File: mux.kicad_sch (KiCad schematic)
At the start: 11 parts, among them M1 SN74LV4051ADYYR, M10 SN74LV4051ADYYR, M11 SN74LV4051ADYYR, M2 SN74LV4051ADYYR, M3 SN74LV4051ADYYR, M4 SN74LV4051ADYYR, M5 SN74LV4051ADYYR, M6 SN74LV4051ADYYR, M7 SN74LV4051ADYYR, M8 SN74LV4051ADYYR, M9 SN74LV4051ADYYR

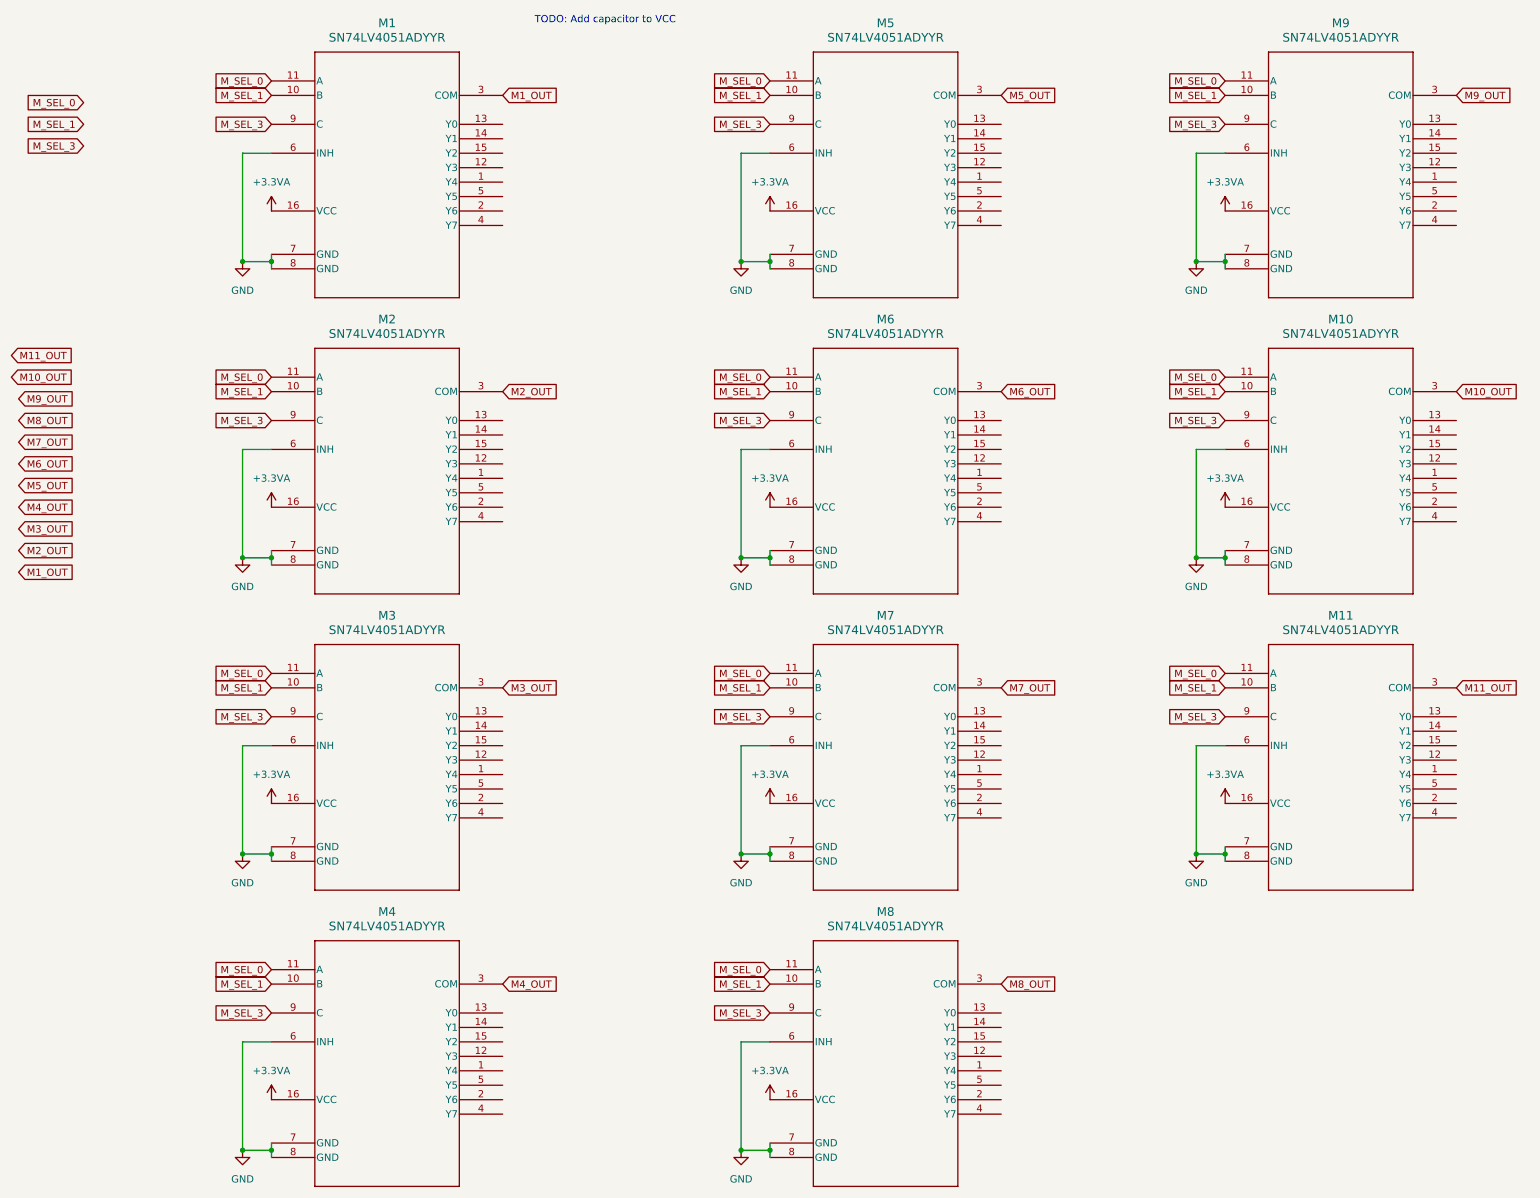
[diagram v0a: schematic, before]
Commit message: start keyboard switch layout
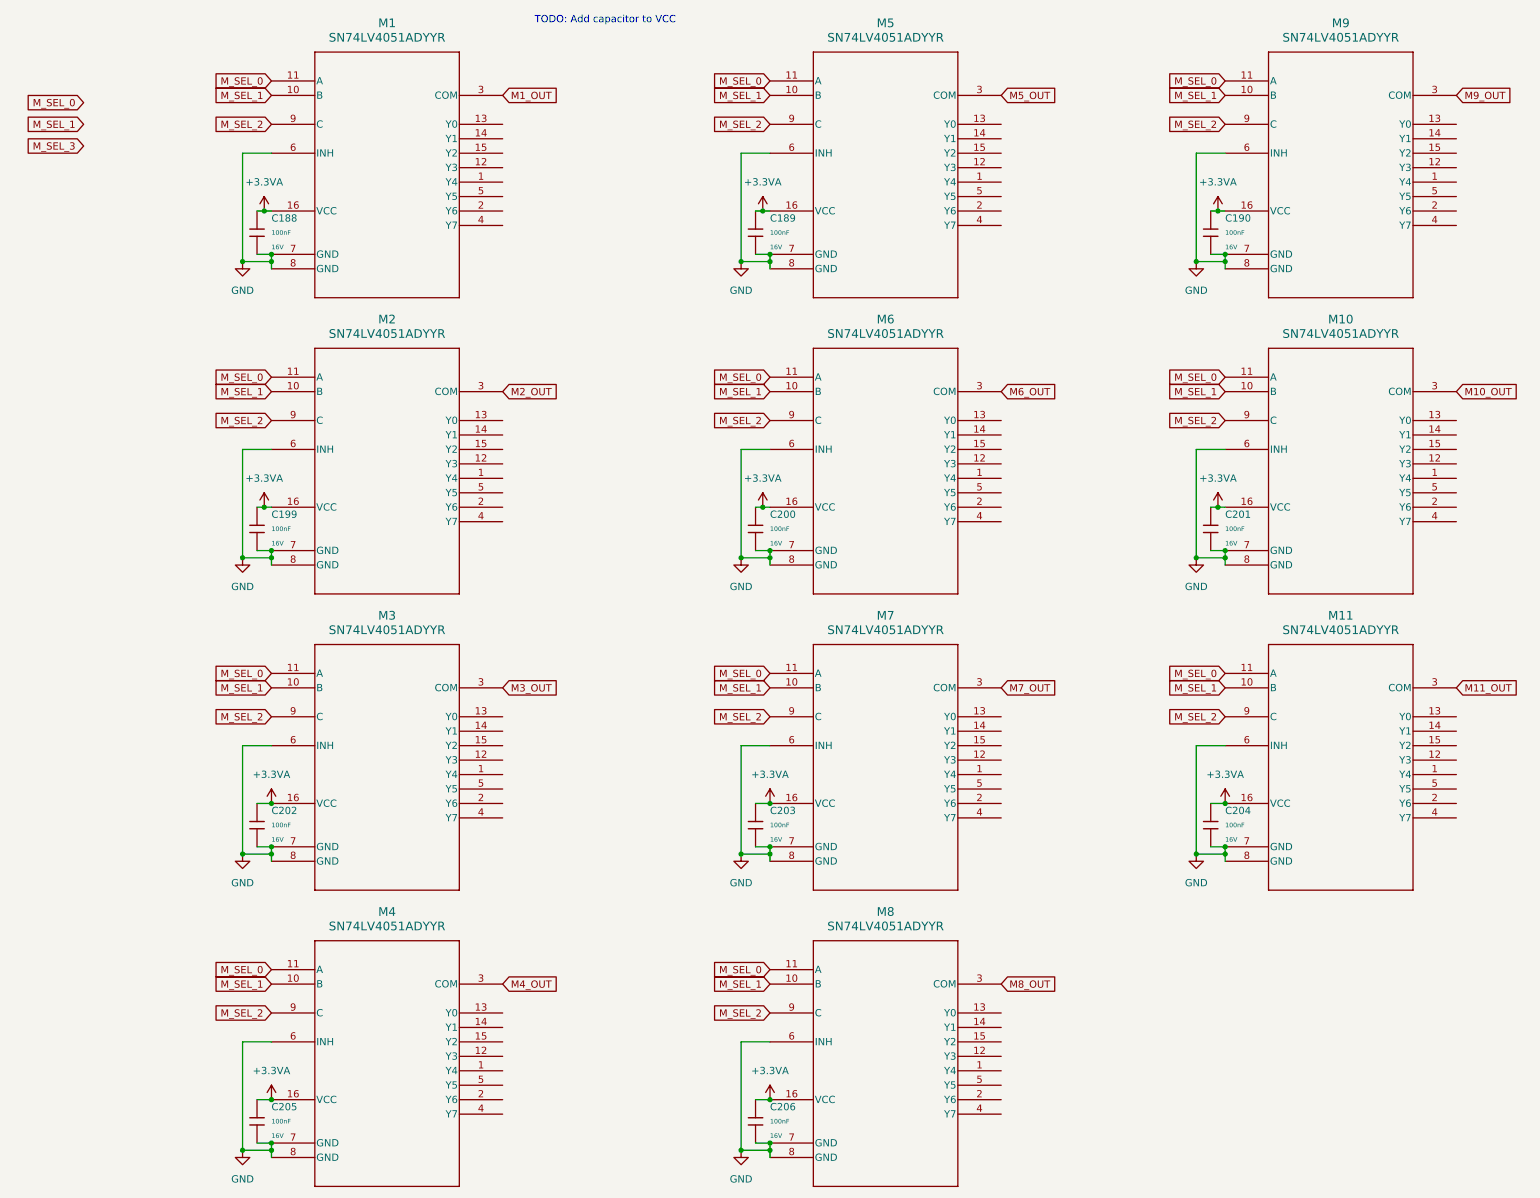
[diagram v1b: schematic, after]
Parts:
- added C188, C189, C190, C199, C200, C201, C202, C203, C204, C205, C206: 100nF, PCM_JLCPCB:C_0402, symbol PCM_JLCPCB-Capacitors:0402,100nF
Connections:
- net +3.3VA: now also C188.1, C189.1, C190.1, C199.1, C200.1, C201.1, C202.1, C203.1, C204.1, C205.1, C206.1
- net GND: now also C188.2, C189.2, C190.2, C199.2, C200.2, C201.2, C202.2, C203.2, C204.2, C205.2, C206.2
- net M_SEL_3: no longer M1.9 (C), M10.9 (C), M11.9 (C), M2.9 (C), M3.9 (C), M4.9 (C), M5.9 (C), M6.9 (C), M7.9 (C), M8.9 (C), M9.9 (C)
- new net M_SEL_2: M1.9 (C), M10.9 (C), M11.9 (C), M2.9 (C), M3.9 (C), M4.9 (C), M5.9 (C), M6.9 (C), M7.9 (C), M8.9 (C), M9.9 (C)

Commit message: final switch layout
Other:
- note removed: "TODO: Add capacitor to VCC"
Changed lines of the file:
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@@
 		(title "Multiplexers")
-	)
-	(text "TODO: Add capacitor to VCC"
-		(exclude_from_sim no)
-		(at 87.884 18.542 0)
-		(effects
-			(font
-				(size 1.27 1.27)
-			)
-		)
 	)
 	(junction

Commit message: add capacitor to mux vcc
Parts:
- renumbered C188 to C201, C199 to C202, C202 to C203, C205 to C204, C189 to C205, C200 to C206, C203 to C209, C206 to C210, C190 to C211, C201 to C212, C204 to C213
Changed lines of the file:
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@@
 		(dnp no)
 		(fields_autoplaced yes)
-		(property "Reference" "C206"
+		(property "Reference" "C210"
 			(at 116.84 209.5499 0)
 			(effects
@@
 			(project "75he"
 				(path "/0edb4e17-93a4-4f7b-ad91-3a5c72b69d23/6cd62204-e1e2-4b31-86d5-519042c12041"
-					(reference "C206")
+					(reference "C210")
 					(unit 1)
 				)
@@
 		(dnp no)
 		(fields_autoplaced yes)
-		(property "Reference" "C188"
+		(property "Reference" "C201"
 			(at 29.21 53.3399 0)
 			(effects
@@
 			(project "75he"
 				(path "/0edb4e17-93a4-4f7b-ad91-3a5c72b69d23/6cd62204-e1e2-4b31-86d5-519042c12041"
-					(reference "C188")
+					(reference "C201")
 					(unit 1)
 				)
@@
 		(dnp no)
 		(fields_autoplaced yes)
-		(property "Reference" "C201"
+		(property "Reference" "C212"
 			(at 196.85 105.4099 0)
 			(effects
@@
 			(project "75he"
 				(path "/0edb4e17-93a4-4f7b-ad91-3a5c72b69d23/6cd62204-e1e2-4b31-86d5-519042c12041"
-					(reference "C201")
+					(reference "C212")
 					(unit 1)
 				)
@@
 		(dnp no)
 		(fields_autoplaced yes)
-		(property "Reference" "C200"
+		(property "Reference" "C206"
 			(at 116.84 105.4099 0)
 			(effects
@@
 			(project "75he"
 				(path "/0edb4e17-93a4-4f7b-ad91-3a5c72b69d23/6cd62204-e1e2-4b31-86d5-519042c12041"
-					(reference "C200")
+					(reference "C206")
 					(unit 1)
 				)
@@
 		(dnp no)
 		(fields_autoplaced yes)
-		(property "Reference" "C190"
+		(property "Reference" "C211"
 			(at 196.85 53.3399 0)
 			(effects
@@
 			(project "75he"
 				(path "/0edb4e17-93a4-4f7b-ad91-3a5c72b69d23/6cd62204-e1e2-4b31-86d5-519042c12041"
-					(reference "C190")
+					(reference "C211")
 					(unit 1)
 				)
@@
 		(dnp no)
 		(fields_autoplaced yes)
-		(property "Reference" "C203"
+		(property "Reference" "C209"
 			(at 116.84 157.4799 0)
 			(effects
@@
 			(project "75he"
 				(path "/0edb4e17-93a4-4f7b-ad91-3a5c72b69d23/6cd62204-e1e2-4b31-86d5-519042c12041"
-					(reference "C203")
+					(reference "C209")
 					(unit 1)
 				)
@@
 		(dnp no)
 		(fields_autoplaced yes)
-		(property "Reference" "C202"
+		(property "Reference" "C203"
 			(at 29.21 157.4799 0)
 			(effects
@@
 			(project "75he"
 				(path "/0edb4e17-93a4-4f7b-ad91-3a5c72b69d23/6cd62204-e1e2-4b31-86d5-519042c12041"
-					(reference "C202")
+					(reference "C203")
 					(unit 1)
 				)
@@
 		(dnp no)
 		(fields_autoplaced yes)
-		(property "Reference" "C199"
+		(property "Reference" "C202"
 			(at 29.21 105.4099 0)
 			(effects
@@
 			(project "75he"
 				(path "/0edb4e17-93a4-4f7b-ad91-3a5c72b69d23/6cd62204-e1e2-4b31-86d5-519042c12041"
-					(reference "C199")
+					(reference "C202")
 					(unit 1)
 				)
@@
 		(dnp no)
 		(fields_autoplaced yes)
-		(property "Reference" "C189"
+		(property "Reference" "C205"
 			(at 116.84 53.3399 0)
 			(effects
@@
 			(project "75he"
 				(path "/0edb4e17-93a4-4f7b-ad91-3a5c72b69d23/6cd62204-e1e2-4b31-86d5-519042c12041"
-					(reference "C189")
+					(reference "C205")
 					(unit 1)
 				)
@@
 		(dnp no)
 		(fields_autoplaced yes)
-		(property "Reference" "C205"
+		(property "Reference" "C204"
 			(at 29.21 209.5499 0)
 			(effects
@@
 			(project "75he"
 				(path "/0edb4e17-93a4-4f7b-ad91-3a5c72b69d23/6cd62204-e1e2-4b31-86d5-519042c12041"
-					(reference "C205")
+					(reference "C204")
 					(unit 1)
 				)
@@
 		(dnp no)
 		(fields_autoplaced yes)
-		(property "Reference" "C204"
+		(property "Reference" "C213"
 			(at 196.85 157.4799 0)
 			(effects
@@
 			(project "75he"
 				(path "/0edb4e17-93a4-4f7b-ad91-3a5c72b69d23/6cd62204-e1e2-4b31-86d5-519042c12041"
-					(reference "C204")
+					(reference "C213")
 					(unit 1)
 				)

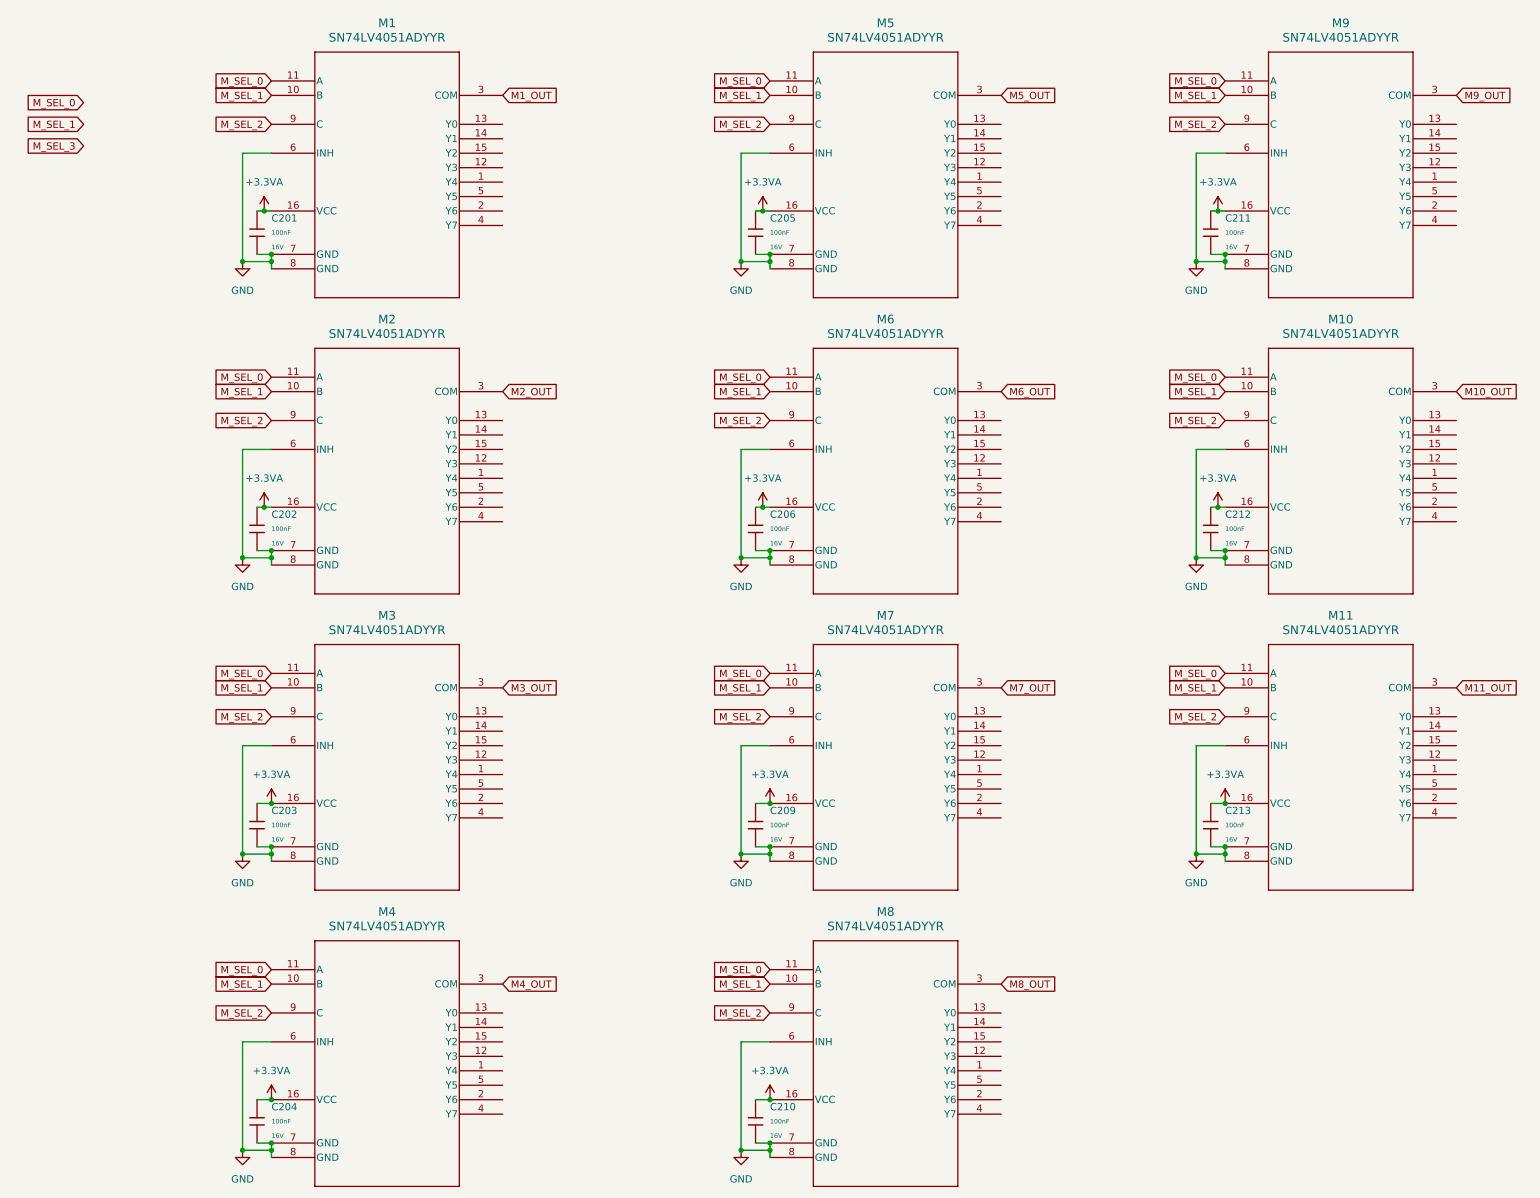
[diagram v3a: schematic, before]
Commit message: start placing mcu capacitor
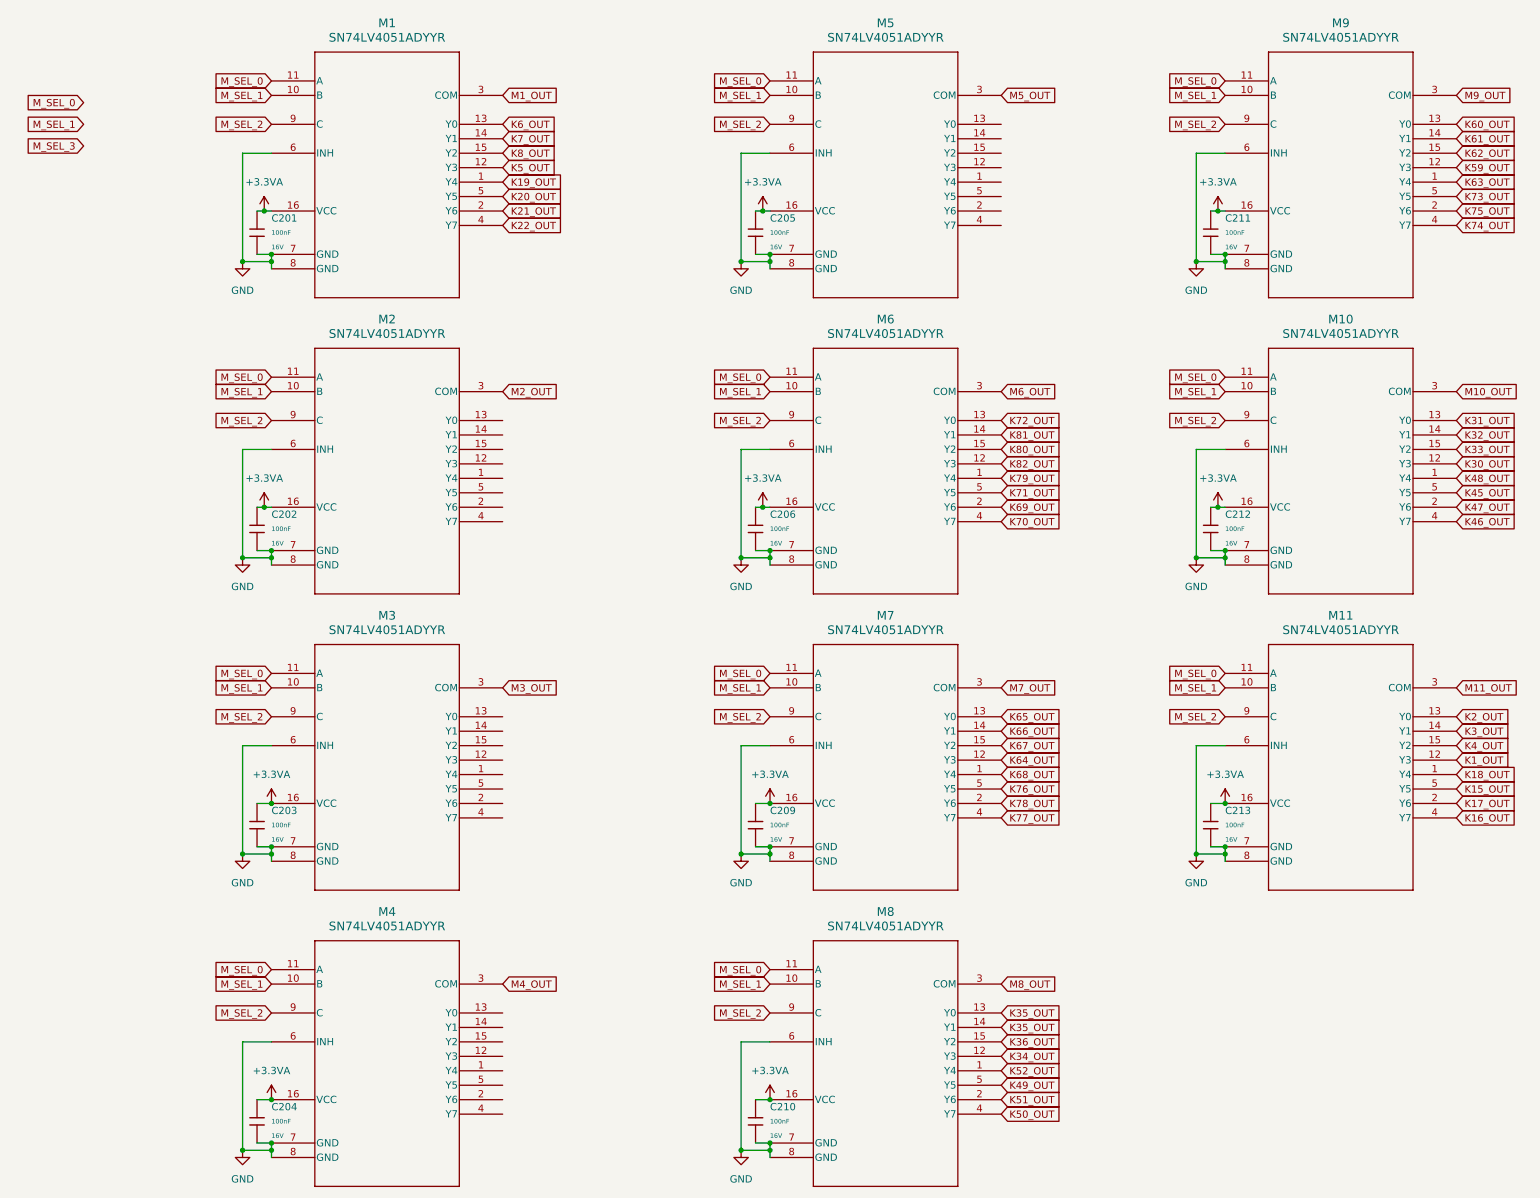
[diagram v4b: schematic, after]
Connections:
- net K52_OUT: now reaches M8.1 (Y4)
- net K34_OUT: now reaches M8.12 (Y3)
- net K35_OUT: now reaches M8.13 (Y0)
- net K35_OUT: now also M8.14 (Y1)
- net K36_OUT: now reaches M8.15 (Y2)
- net K51_OUT: now reaches M8.2 (Y6)
- net K50_OUT: now reaches M8.4 (Y7)
- net K49_OUT: now reaches M8.5 (Y5)
- net K19_OUT: now reaches M1.1 (Y4)
- net K5_OUT: now reaches M1.12 (Y3)
- net K6_OUT: now reaches M1.13 (Y0)
- net K7_OUT: now reaches M1.14 (Y1)
- net K8_OUT: now reaches M1.15 (Y2)
- net K21_OUT: now reaches M1.2 (Y6)
- net K22_OUT: now reaches M1.4 (Y7)
- net K20_OUT: now reaches M1.5 (Y5)
- net K63_OUT: now reaches M9.1 (Y4)
- net K59_OUT: now reaches M9.12 (Y3)
- net K60_OUT: now reaches M9.13 (Y0)
- net K61_OUT: now reaches M9.14 (Y1)
- net K62_OUT: now reaches M9.15 (Y2)
- net K75_OUT: now reaches M9.2 (Y6)
- net K74_OUT: now reaches M9.4 (Y7)
- net K73_OUT: now reaches M9.5 (Y5)
- net K79_OUT: now reaches M6.1 (Y4)
- net K82_OUT: now reaches M6.12 (Y3)
- net K72_OUT: now reaches M6.13 (Y0)
- net K81_OUT: now reaches M6.14 (Y1)
- net K80_OUT: now reaches M6.15 (Y2)
- net K69_OUT: now reaches M6.2 (Y6)
- net K70_OUT: now reaches M6.4 (Y7)
- net K71_OUT: now reaches M6.5 (Y5)
- net K68_OUT: now reaches M7.1 (Y4)
- net K64_OUT: now reaches M7.12 (Y3)
- net K65_OUT: now reaches M7.13 (Y0)
- net K66_OUT: now reaches M7.14 (Y1)
- net K67_OUT: now reaches M7.15 (Y2)
- net K78_OUT: now reaches M7.2 (Y6)
- net K77_OUT: now reaches M7.4 (Y7)
- net K76_OUT: now reaches M7.5 (Y5)
- net K18_OUT: now reaches M11.1 (Y4)
- net K1_OUT: now reaches M11.12 (Y3)
- net K2_OUT: now reaches M11.13 (Y0)
- net K3_OUT: now reaches M11.14 (Y1)
- net K4_OUT: now reaches M11.15 (Y2)
- net K17_OUT: now reaches M11.2 (Y6)
- net K16_OUT: now reaches M11.4 (Y7)
- net K15_OUT: now reaches M11.5 (Y5)
- net K48_OUT: now reaches M10.1 (Y4)
- net K30_OUT: now reaches M10.12 (Y3)
- net K31_OUT: now reaches M10.13 (Y0)
- net K32_OUT: now reaches M10.14 (Y1)
- net K33_OUT: now reaches M10.15 (Y2)
- net K47_OUT: now reaches M10.2 (Y6)
- net K46_OUT: now reaches M10.4 (Y7)
- net K45_OUT: now reaches M10.5 (Y5)
